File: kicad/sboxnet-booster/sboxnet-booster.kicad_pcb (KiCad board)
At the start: 2 copper layers, 56 parts, among them J1 sboxnet-stecker_02x17, J2 Conn_01x02_Male, J3 Conn_01x02_Male, J4 Conn_01x02_Male, J5 Screw_Terminal_01x04, J6 Screw_Terminal_01x04, J7 Power von externen 15V/4A Net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, SW1 Öffner, U1 l6206

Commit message: update booster kicad
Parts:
- removed REF** (x3): MountingHole_2.2mm_M2, sboxnet:MountingHole_2.2mm_M2
- added R11: 10k, Resistor_THT:R_Axial_DIN0204_L3.6mm_D1.6mm_P7.62mm_Horizontal, F.Cu at (57.3, 14.9)
- added R12: 10k, Resistor_THT:R_Axial_DIN0204_L3.6mm_D1.6mm_P7.62mm_Horizontal, F.Cu at (57.3, 18.1)
- U1: value l6206 -> L6206PSO; footprint sboxnet:POWERSO36 -> Package_SO:HSOP-36-1EP_11.0x15.9mm_P0.65mm_SlugDown_ThermalVias
- moved U1 8.89 mm to (79.9, 111.8)
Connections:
- C2 pad 2: Net-(C2-Pad2) -> VBOOT
- C3 pad 1: Net-(C3-Pad1) -> VCP
- D10 pad 2: Net-(D10-Pad2) -> OUT1a
- D8 pad 1: Net-(C2-Pad2) -> VBOOT
- D9 pad 1: Net-(D10-Pad2) -> OUT1a
- J3 pad 1: Net-(J3-Pad1) -> OUT2b
- J3 pad 2: Net-(J3-Pad2) -> OUT2a
- J4 pad 1: Net-(J4-Pad1) -> OUT1b
- J4 pad 2: Net-(D10-Pad2) -> OUT1a
- J5 pad 1: Net-(J3-Pad2) -> OUT2a
- J5 pad 2: Net-(J3-Pad2) -> OUT2a
- J5 pad 3: Net-(J3-Pad2) -> OUT2a
- J5 pad 4: Net-(J3-Pad2) -> OUT2a
- J6 pad 1: Net-(D10-Pad2) -> OUT1a
- J6 pad 2: Net-(D10-Pad2) -> OUT1a
- J6 pad 3: Net-(D10-Pad2) -> OUT1a
- J6 pad 4: Net-(D10-Pad2) -> OUT1a
- R16 pad 1: Net-(J3-Pad2) -> OUT2a
- R17 pad 1: Net-(J3-Pad2) -> OUT2a
- R17 pad 2: Net-(D10-Pad2) -> OUT1a
- U1 pad 1: IN1 -> GND
- U1 pad 10: SENSE -> IN1
- U1 pad 12: IN1 -> GND
- U1 pad 13: Net-(R14-Pad2) -> PC3
- U1 pad 14: EN -> (no net)
- U1 pad 15: Net-(C2-Pad2) -> OUT1a
- U1 pad 16: Net-(J3-Pad1) -> (no net)
- U1 pad 17: V -> (no net)
- U1 pad 2: IN2 -> (no net)
- U1 pad 20: V -> (no net)
- U1 pad 21: Net-(J3-Pad2) -> (no net)
- U1 pad 22: Net-(C3-Pad1) -> OUT1b
- U1 pad 23: EN -> (no net)
- U1 pad 24: Net-(R15-Pad2) -> PC3
- U1 pad 25: (no net) -> GND
- U1 pad 26: (no net) -> IN1
- U1 pad 27: (no net) -> IN2
- U1 pad 28: (no net) -> Net-(R12-Pad2)
- U1 pad 29: (no net) -> EN
- U1 pad 3: SENSE -> (no net)
- U1 pad 30: (no net) -> VBOOT
- U1 pad 32: (no net) -> OUT2b
- U1 pad 33: (no net) -> V
- U1 pad 36: (no net) -> GND
- U1 pad 4: PC3 -> V
- U1 pad 5: Net-(D10-Pad2) -> OUT2a
- U1 pad 6: GND -> (no net)
- U1 pad 7: GND -> VCP
- U1 pad 8: Net-(J4-Pad1) -> EN
- U1 pad 9: PC3 -> Net-(R11-Pad1)
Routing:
- net Net-(J1-Pad2): track 56.4 -> 0.00 mm
- net PC3: track 0.00 -> 51.1 mm
- net PC2: track 44.1 -> 0.00 mm
- net IN2: track 36.9 -> 0.00 mm
- net IN1: track 33.3 -> 0.00 mm

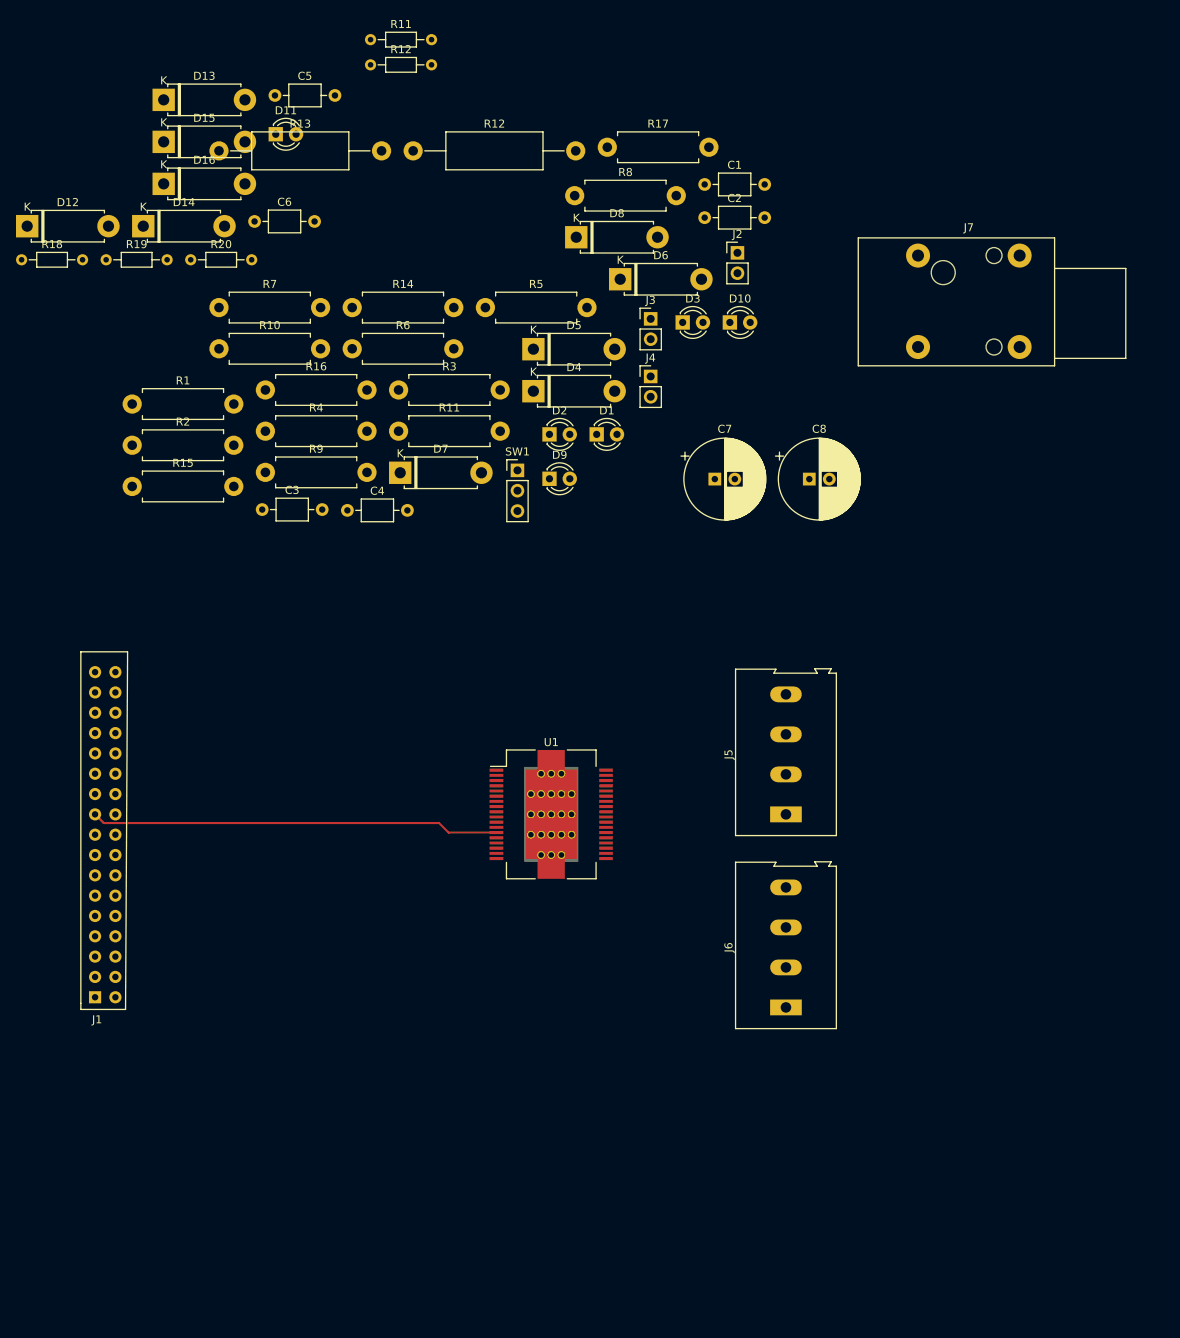
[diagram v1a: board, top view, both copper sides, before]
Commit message: update booster layout with POWERSO Slug Down Terminal Vias
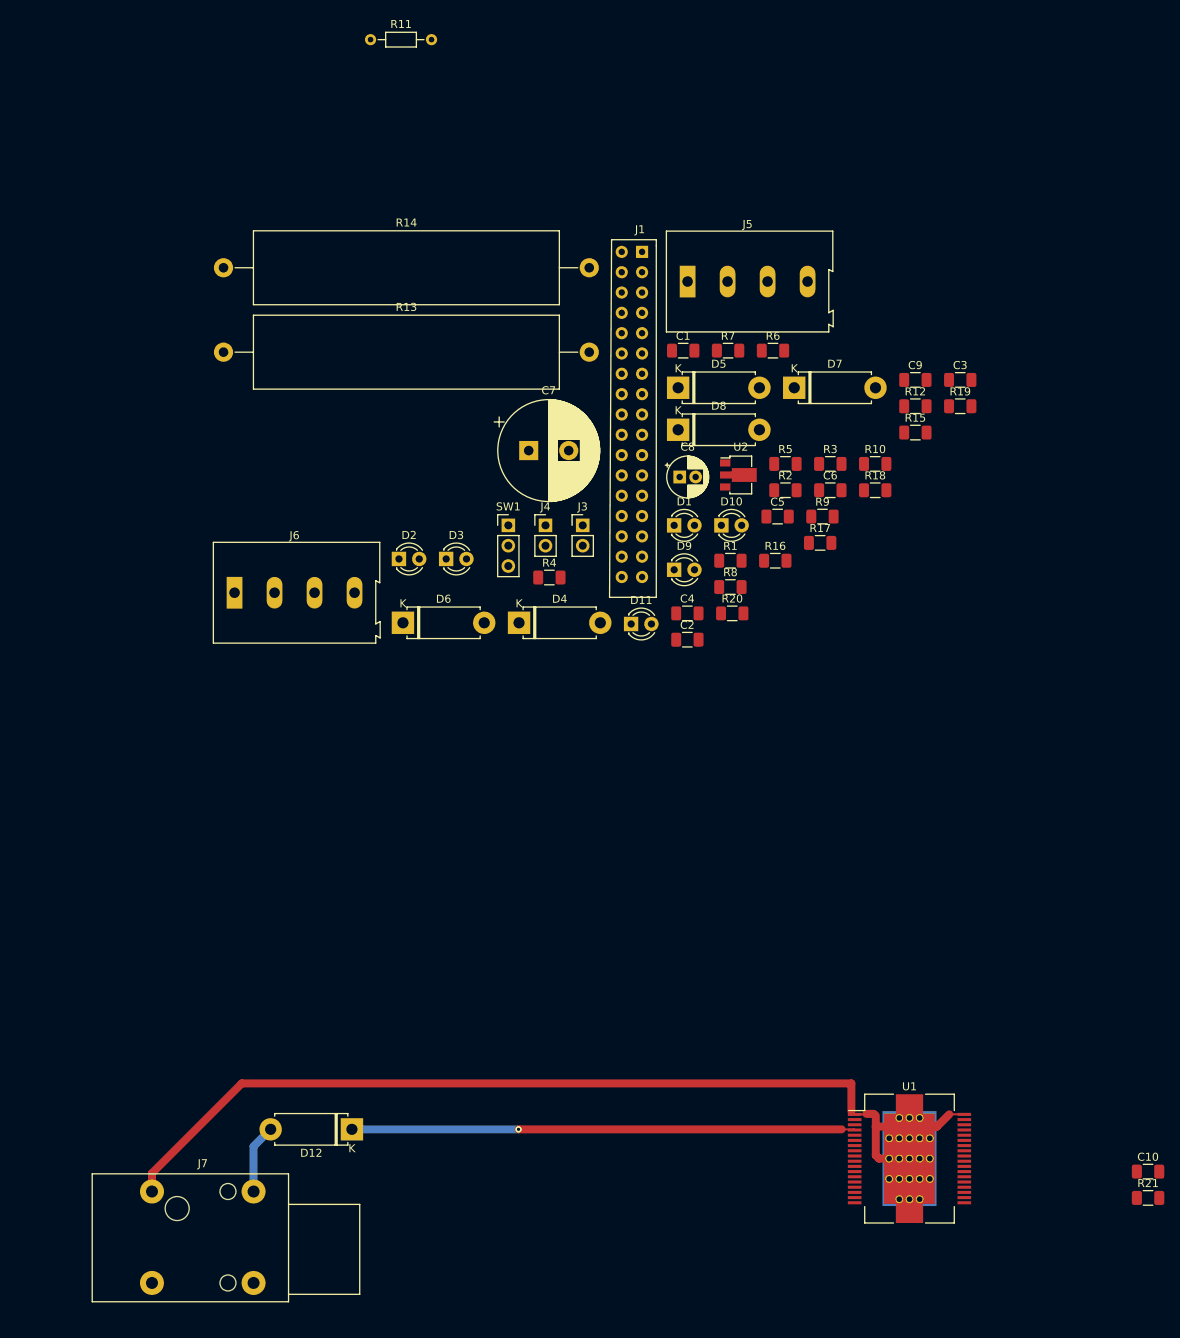
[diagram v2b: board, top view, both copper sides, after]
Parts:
- removed D13, D14, D15, D16: 1N4001, Diode_THT:D_5W_P10.16mm_Horizontal
- removed J2: Conn_01x02_Male, Connector_PinHeader_2.54mm:PinHeader_1x02_P2.54mm_Vertical
- removed the R11 at (60.8, 63.9)
- removed the R12 at (57.3, 18.1)
- removed the R12 at (62.6, 28.8)
- added C10: 1u, Capacitor_SMD:C_1206_3216Metric, F.Cu at (154.5, 156.4)
- added C9: 1u, Capacitor_SMD:C_1206_3216Metric, F.Cu at (125.4, 57.5)
- added R12: 10k, Resistor_SMD:R_1206_3216Metric, F.Cu at (125.4, 60.7)
- added R21: 10k, Resistor_SMD:R_1206_3216Metric, F.Cu at (154.5, 159.7)
- added U2: L78L12_SOT89, Package_TO_SOT_SMD:SOT-89-3, F.Cu at (103.3, 69.3)
- C1, C2, C3, C4, C5, C6: footprint Capacitor_THT:C_Axial_L3.8mm_D2.6mm_P7.50mm_Horizontal -> Capacitor_SMD:C_1206_3216Metric
- C7: footprint Capacitor_THT:CP_Radial_D10.0mm_P2.50mm -> Capacitor_THT:CP_Radial_D12.5mm_P5.00mm
- C8: footprint Capacitor_THT:CP_Radial_D10.0mm_P2.50mm -> Capacitor_THT:CP_Radial_D5.0mm_P2.00mm
- D12: value 1N4001 -> NTE 5812HC 10A
- R1, R10, R15, R16, R17, R2, R3, R4, R5, R6, R7, R8, R9: footprint Resistor_THT:R_Axial_DIN0411_L9.9mm_D3.6mm_P12.70mm_Horizontal -> Resistor_SMD:R_1206_3216Metric
- R13: value 0.25 / 2W -> 0.22; footprint Resistor_THT:R_Axial_DIN0414_L11.9mm_D4.5mm_P20.32mm_Horizontal -> Resistor_THT:R_Axial_Power_L38.0mm_W9.0mm_P45.72mm
- R14: value 10k -> 0.22; footprint Resistor_THT:R_Axial_DIN0411_L9.9mm_D3.6mm_P12.70mm_Horizontal -> Resistor_THT:R_Axial_Power_L38.0mm_W9.0mm_P45.72mm
- R18, R19, R20: footprint Resistor_THT:R_Axial_DIN0204_L3.6mm_D1.6mm_P7.62mm_Horizontal -> Resistor_SMD:R_1206_3216Metric
- U1: value L6206PSO -> L6206PSO-sboxnet
- moved J7 151.2 mm to (30.0, 158.9)
- moved D12 120.0 mm to (55.0, 151.1), turned to 180 degrees
- moved J1 116.9 mm to (88.7, 38.9), turned to 0 degrees
- moved R18 110.5 mm to (120.4, 71.2)
- moved R19 108.3 mm to (131.0, 60.7)
- moved R15 98.1 mm to (125.4, 64.0)
- moved C3 88.7 mm to (131.0, 57.5)
- moved J6 86.2 mm to (40.3, 84.1), turned to 0 degrees
- moved R10 83.3 mm to (120.4, 68.0)
- moved C5 82.0 mm to (108.2, 74.5)
- moved R2 81.8 mm to (109.2, 71.2)
- moved R20 80.8 mm to (102.5, 86.6)
- moved C6 79.4 mm to (114.8, 71.2)
- moved R1 77.3 mm to (102.3, 80.1)
- moved D11 75.6 mm to (89.9, 88.0)
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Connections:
- C4 pad 2: PA0 -> V
- C8 pad 1: Net-(C8-Pad1) -> +12V
- J1 pad 7: Net-(J1-Pad7) -> PA2
- R13 pad 1: SENSE -> Net-(R13-Pad1)
- R15 pad 1: GND -> Net-(R13-Pad1)
- R15 pad 2: Net-(R15-Pad2) -> PA0
- U1 pad 12: GND -> Net-(R13-Pad1)
- U1 pad 25: GND -> Net-(R14-Pad2)
- U1 pad 37: (no net) -> GND
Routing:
- net GND: track 0.00 -> 122.2 mm
- net V: track 0.00 -> 62.9 mm, vias 0 -> 1
- net PC3: track 51.1 -> 0.00 mm
- net Net-(D12-Pad2): track 0.00 -> 8.66 mm

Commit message: fixed
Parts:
- moved J1 122.2 mm to (21.5, 141.0), turned to 180 degrees
- moved C6 96.4 mm to (36.1, 126.9)
- moved C7 80.5 mm to (38.5, 136.9), turned to 180 degrees
- moved D7 77.6 mm to (70.9, 125.3)
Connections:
- J1 pad 2: Net-(J1-Pad2) -> GND
- J1 pad 3: +5V -> +3V3
- J1 pad 4: +3V3 -> +5V
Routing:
- net GND: track 122.2 -> 170.7 mm
- net V: track 62.9 -> 95.7 mm

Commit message: PSO backplane
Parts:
- C1: value 10n -> 100n
- D4, D5, D6: value BAT48 -> BAR42FILM; footprint Diode_THT:D_5W_P10.16mm_Horizontal -> Package_TO_SOT_SMD:SOT-23
- D7, D8: value 1N4148 -> 1N4148WS; footprint Diode_THT:D_5W_P10.16mm_Horizontal -> Diode_SMD:D_SOD-323
- R11: footprint Resistor_THT:R_Axial_DIN0204_L3.6mm_D1.6mm_P7.62mm_Horizontal -> Resistor_SMD:R_1206_3216Metric
- moved J1 132.7 mm to (75.4, 19.7), turned to 0 degrees
- moved C10 122.9 mm to (89.2, 52.2)
- moved R21 117.2 mm to (85.6, 64.9)
- moved J5 113.1 mm to (118.1, 156.2)
- moved D7 109.2 mm to (116.1, 26.0)
- moved C7 93.3 mm to (63.8, 47.1), turned to 0 degrees
- moved D6 77.1 mm to (115.9, 33.4)
- moved J6 74.4 mm to (58.4, 156.2)
- moved J4 73.3 mm to (93.3, 147.6), turned to 270 degrees
- moved J3 72.2 mm to (110.0, 142.9), turned to 270 degrees
- moved D3 64.5 mm to (104.2, 27.3)
- moved C6 63.5 mm to (63.2, 69.5)
- moved C4 62.1 mm to (111.2, 26.2)
- moved D9 61.3 mm to (110.1, 21.7)
- moved R11 57.0 mm to (110.3, 36.0)
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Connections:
- C1 pad 1: GND -> Net-(C1-Pad1)
- C1 pad 2: Net-(C1-Pad2) -> GND
- D4 pad 1: Net-(D4-Pad1) -> PC2
- D4 pad 2: PC2 -> Net-(D4-Pad2)
- D5 pad 1: PC2 -> EN
- D5 pad 2: EN -> Net-(D5-Pad2)
- D6 pad 1: PC3 -> Net-(C1-Pad1)
- D6 pad 2: Net-(C1-Pad2) -> Net-(D6-Pad2)
- R8 pad 1: Net-(D4-Pad1) -> Net-(D4-Pad3)
- R8 pad 2: Net-(C1-Pad2) -> Net-(C1-Pad1)
- R9 pad 1: Net-(C1-Pad2) -> Net-(C1-Pad1)
- SW1 pad 2: GND -> Net-(SW1-Pad2)
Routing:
- net GND: track 170.7 -> 62.2 mm
- net OUT2a: track 0.00 -> 95.3 mm, vias 0 -> 2
- net OUT1a: track 0.00 -> 68.6 mm, vias 0 -> 1
- net OUT1b: track 0.00 -> 31.3 mm, vias 0 -> 1
- net OUT2b: track 0.00 -> 19.7 mm
- net V: track 95.7 -> 83.7 mm, vias 1 -> 2
- added copper zone on F.Cu, net GND

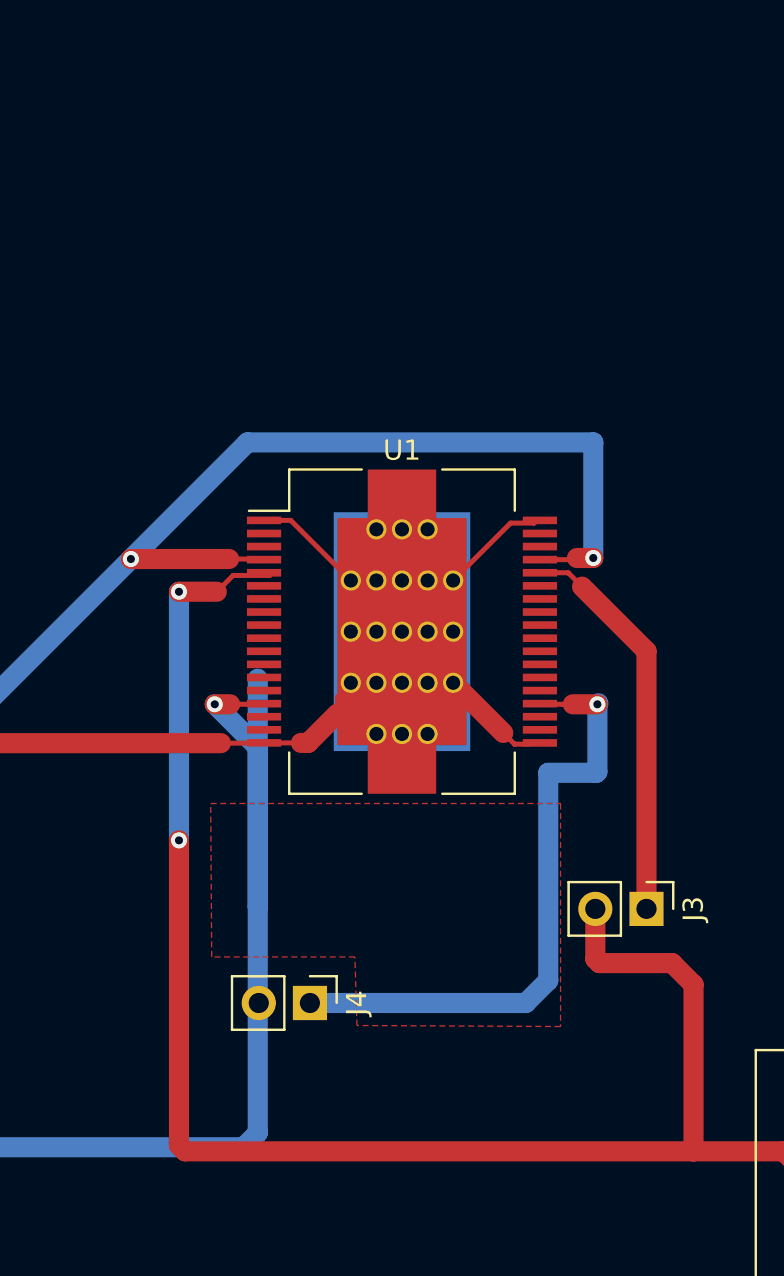
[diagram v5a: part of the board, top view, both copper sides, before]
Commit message: add heatsink footprint
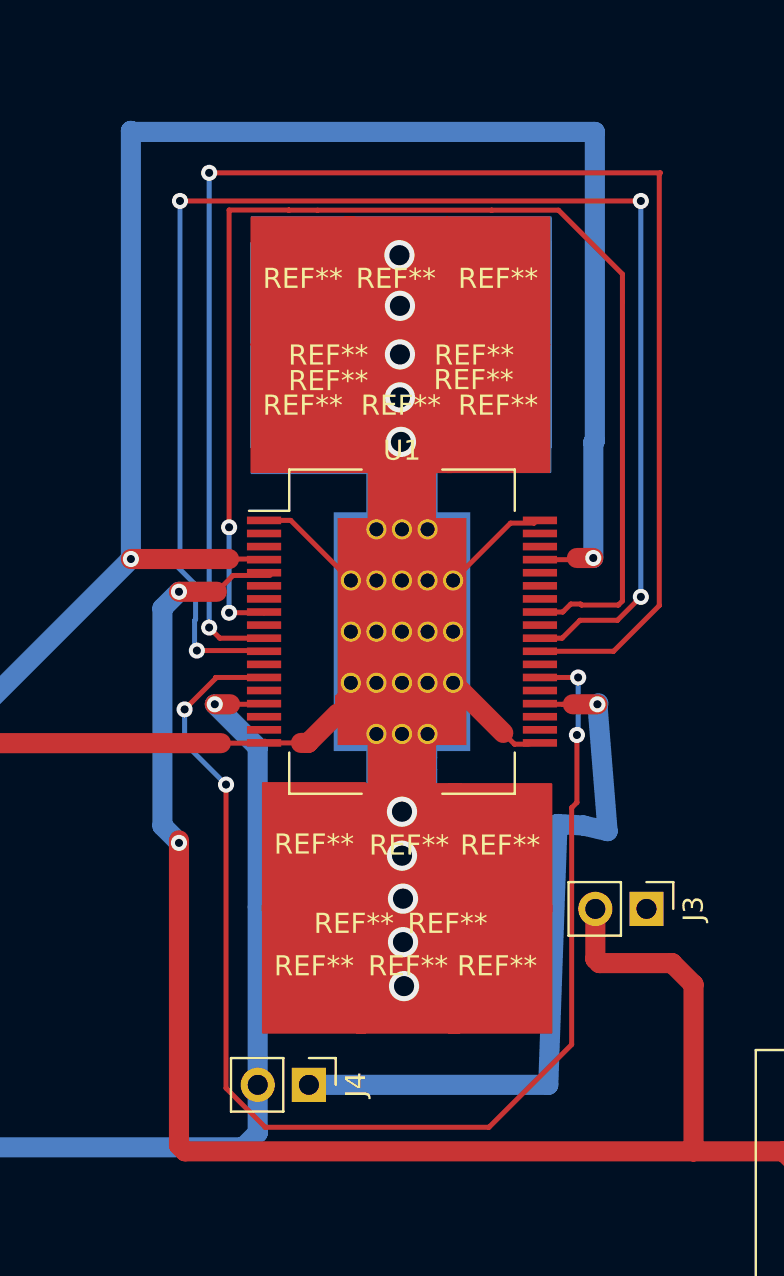
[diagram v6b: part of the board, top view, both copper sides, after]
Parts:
- added REF**: hs_b, sboxnet:heatsink_b, F.Cu at (95.5, 143.1)
- added REF**: heatsink, sboxnet:heatsink, F.Cu at (102.7, 117.4)
- added REF**: heatsink, sboxnet:heatsink, F.Cu at (93.0, 117.4)
- added REF**: heatsink, sboxnet:heatsink, F.Cu at (97.8, 117.4)
- added REF**: heatsink, sboxnet:heatsink, F.Cu at (102.8, 145.2)
- added REF**: heatsink, sboxnet:heatsink, F.Cu at (93.5, 145.2)
- added REF**: heatsink, sboxnet:heatsink, F.Cu at (98.2, 145.2)
- added REF**: heatsink, sboxnet:heatsink, F.Cu at (102.8, 139.2)
- added REF**: heatsink, sboxnet:heatsink, F.Cu at (93.5, 139.2)
- added REF**: heatsink, sboxnet:heatsink, F.Cu at (98.2, 139.2)
- added REF**: hs_b, sboxnet:heatsink_b, F.Cu at (100.2, 143.1)
- added REF**: hs_b, sboxnet:heatsink_b, F.Cu at (101.5, 114.9)
- added REF**: hs_b, sboxnet:heatsink_b, F.Cu at (94.2, 114.9)
- added REF**: hs_b, sboxnet:heatsink_b, F.Cu at (94.2, 116.2)
- added REF**: hs_b, sboxnet:heatsink_b, F.Cu at (101.4, 116.1)
- added REF**: heatsink, sboxnet:heatsink, F.Cu at (93.0, 111.1)
- added REF**: heatsink, sboxnet:heatsink, F.Cu at (97.6, 111.1)
- added REF**: heatsink, sboxnet:heatsink, F.Cu at (102.7, 111.1)
- moved J4 4.06 mm to (93.3, 151.6)
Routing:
- net IN1: track 0.00 -> 76.3 mm, vias 0 -> 2
- net IN2: track 0.00 -> 74.6 mm, vias 0 -> 4
- net PC3: track 0.00 -> 64.2 mm, vias 0 -> 4
- net EN: track 0.00 -> 63.2 mm, vias 0 -> 2
- net GND: track 62.2 -> 107.2 mm
- net V: track 83.7 -> 118.1 mm
- net OUT2b: track 19.7 -> 0.00 mm
- net OUT1a: track 68.6 -> 57.3 mm
- net OUT1b: track 31.3 -> 36.6 mm
- net OUT2a: track 95.3 -> 96.0 mm
- net (no net): vias 0 -> 10
- removed copper zone on F.Cu, net GND

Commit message: work in progress layout
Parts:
- J7: value Power von externen 15V/4A Netzteil -> Power von externen 15V/4A Netzteil DS_NRJ4HF
- moved R14 121.3 mm to (130.6, 85.0), turned to 270 degrees
- moved R13 106.4 mm to (71.4, 130.8), turned to 90 degrees
- moved D7 99.8 mm to (118.7, 125.8)
- moved D8 97.1 mm to (109.8, 125.8)
- moved C7 94.6 mm to (64.3, 141.7)
- moved C3 75.4 mm to (115.4, 117.9), turned to 270 degrees
- moved R10 73.2 mm to (115.4, 122.5), turned to 270 degrees
- moved C2 71.9 mm to (110.3, 118.7), turned to 180 degrees
- moved C6 69.0 mm to (82.3, 135.8), turned to 270 degrees
- moved J1 18.8 mm to (61.0, 31.8), turned to 90 degrees
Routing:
- net GND: track 107.2 -> 211.7 mm, vias 0 -> 1
- net VCP: track 0.00 -> 76.9 mm, vias 0 -> 2
- net V: track 118.1 -> 146.1 mm, vias 2 -> 4
- net Net-(R14-Pad2): track 0.00 -> 26.9 mm
- net OUT2b: track 0.00 -> 19.9 mm, vias 0 -> 1
- net Net-(R13-Pad1): track 0.00 -> 19.3 mm
- net VBOOT: track 0.00 -> 11.8 mm
- net Net-(D7-Pad1): track 0.00 -> 8.84 mm
- net Net-(C3-Pad2): track 0.00 -> 1.87 mm
- net EN: track 63.2 -> 64.7 mm
- net OUT1b: track 36.6 -> 35.9 mm
- added copper zone on F.Cu, net GND
